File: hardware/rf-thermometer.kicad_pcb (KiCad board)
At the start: 4 copper layers, 40.6 x 40.6 mm, 17 parts, among them U1 TDA7100, U2 STM32L011G4Ux

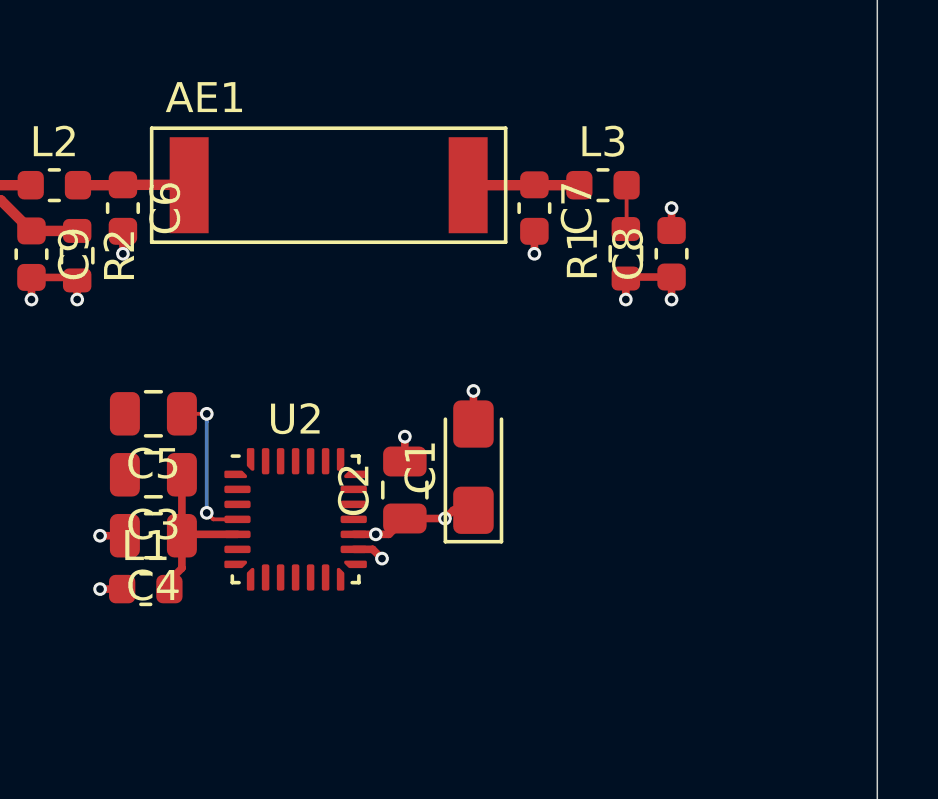
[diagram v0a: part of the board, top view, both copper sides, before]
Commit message: NOTATIONAL add programming header for STM32
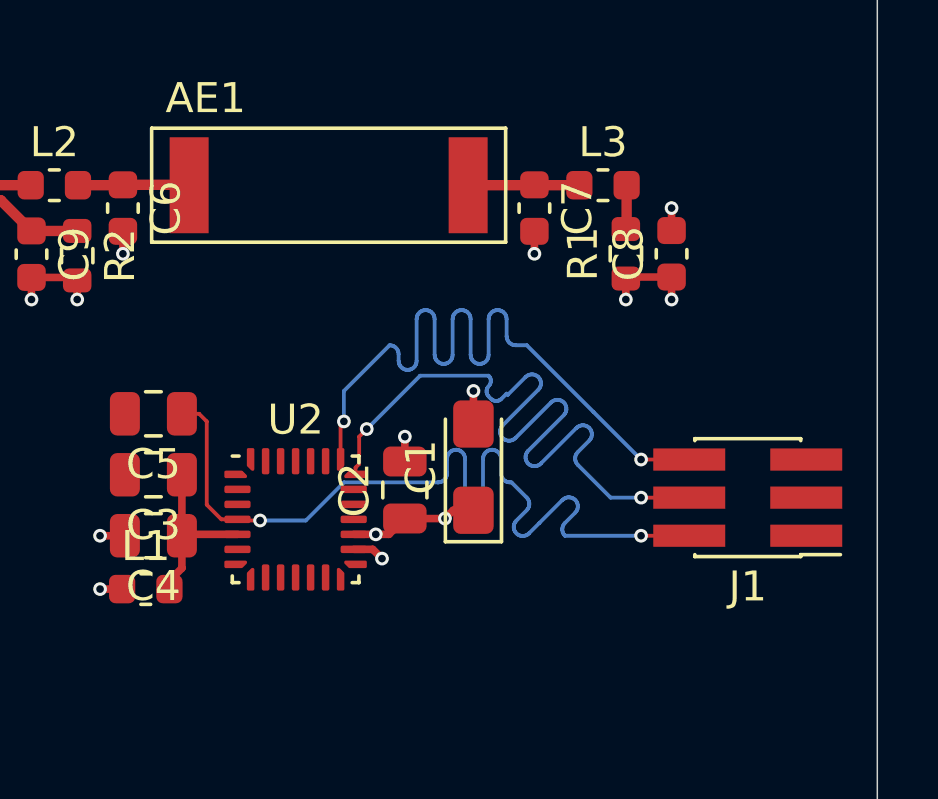
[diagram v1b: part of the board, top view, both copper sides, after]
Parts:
- added J1: Conn_02x03_Odd_Even, Connector_PinHeader_1.27mm:PinHeader_2x03_P1.27mm_Vertical_SMD, F.Cu at (178.6, 105.7)
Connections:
- U1 pad 1: Net-(U1-Pad1) -> (no net)
- U1 pad 10: Net-(U1-Pad10) -> (no net)
- U1 pad 4: Net-(U1-Pad4) -> (no net)
- U1 pad 5: Net-(U1-Pad5) -> (no net)
- U1 pad 6: Net-(U1-Pad6) -> (no net)
- U1 pad 7: Net-(U1-Pad7) -> (no net)
- U2 pad 1: ADC_IN9 -> (no net)
- U2 pad 10: Net-(U2-Pad10) -> (no net)
- U2 pad 11: Net-(U2-Pad11) -> (no net)
- U2 pad 12: Net-(U2-Pad12) -> (no net)
- U2 pad 13: Net-(U2-Pad13) -> (no net)
- U2 pad 14: Net-(U2-Pad14) -> (no net)
- U2 pad 15: Net-(U2-Pad15) -> (no net)
- U2 pad 18: Net-(U2-Pad18) -> (no net)
- U2 pad 19: Net-(U2-Pad19) -> (no net)
- U2 pad 2: Net-(U2-Pad2) -> (no net)
- U2 pad 20: Net-(U2-Pad20) -> (no net)
- U2 pad 23: Net-(U2-Pad23) -> (no net)
- U2 pad 24: Net-(U2-Pad24) -> (no net)
- U2 pad 25: Net-(U2-Pad25) -> (no net)
- U2 pad 26: Net-(U2-Pad26) -> (no net)
- U2 pad 27: Net-(U2-Pad27) -> (no net)
- U2 pad 28: Net-(U2-Pad28) -> (no net)
- U2 pad 3: Net-(U2-Pad3) -> (no net)
- U2 pad 6: USART2_RX -> (no net)
- U2 pad 7: Net-(U2-Pad7) -> (no net)
- U2 pad 8: USART2_TX -> (no net)
- U2 pad 9: Net-(U2-Pad9) -> (no net)
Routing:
- net SWDIO: track 0.00 -> 25.5 mm, vias 0 -> 2
- net SWCLK: track 0.00 -> 25.4 mm, vias 0 -> 2
- net ~RST: track 5.24 -> 30.3 mm
